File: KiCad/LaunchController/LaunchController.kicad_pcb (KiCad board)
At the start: 2 copper layers, 263 parts, among them J1 DC_IN, J10 CONN_SPEAKER, J11 CONN_EXT_I2C_0, J12 CONN_EXT_GPIO_0, J13 CONN_EXT_SPI_0, J14 CONN_EXT_I2C_1, J15 CONN_EXT_GPIO_1, J16 CONN_EXT_SPI_1, J17 CONN_USB, J18 CONN_EXT_I2C_2, J19 CONN_EXT_GPIO_2, J2 JMP_RUN, J20 USB_B_Micro, J21 CONN_EXT_SPI_2, J22 CONN_EXT_I2C_3, J23 CONN_EXT_GPIO_3, J24 JMP_DUMP, J25 JMP_SAFETY, J26 JMP_O2, J27 JMP_EMERGENCY_STOP, J28 JMP_IGNITOR, J29 JMP_SEQUENCE_START, J3 CONN_ICSP, J30 JMP_VALVE_OPEN, J31 JMP_FILL, J32 INDICATOR_PANEL, J33 JMP_VALVE_CLOSE, J34 JMP_PURGE, J35 CONTROL_PANEL, J36 STATUS_PANEL, J4 CONN_RS485, J5 JMP_KILL, J6 CONN_AUDIO, J7 L, J8 R, J9 CONN_EXT_UART, Q1 TJ8S06M3L, Q10 2SC3325-Y, Q11 2SC3325-Y, Q12 2SC3325-Y, Q13 2SC3325-Y, Q14 2SC3325-Y, Q2 TJ8S06M3L, Q3 2SC3325-Y, Q4 2SC3325-Y, Q5 2SC3325-Y, Q6 2SC3325-Y, Q7 2SC3325-Y, Q8 2SC3325-Y, Q9 2SC3325-Y, SW1 SW_RESET, U1 SI-8008HFE, U2 NJM7805SDL1, U3 INA219BIDCNT, U4 INA219BIDCNT, U5 U74HC14, U6 LTC485CN8#PBF, U7 FT232RL, U8 ATMEGA2560-16AUR, U9 U74HC14, Y1 HUSG-16.000-20

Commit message: ボード設計中（地獄）
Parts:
- R14: value 10kR -> 120R
- moved J4 255.6 mm to (261.6, 100.4), turned to -90 degrees
- moved J13 252.7 mm to (255.3, 141.0)
- moved J16 252.3 mm to (255.2, 148.0)
- moved J21 248.3 mm to (255.3, 154.9)
- moved R107 241.0 mm to (261.0, 35.3), turned to -90 degrees
- moved J11 240.0 mm to (241.3, 133.9)
- moved R106 237.6 mm to (258.4, 35.3), turned to -90 degrees
- moved J14 236.9 mm to (241.3, 141.0)
- moved J18 234.1 mm to (241.3, 148.0)
- moved J22 231.5 mm to (241.3, 154.9)
- moved J17 230.6 mm to (261.6, 69.7), turned to -90 degrees
- moved D21 229.3 mm to (263.5, 35.3), turned to -90 degrees
- moved J20 228.8 mm to (261.6, 59.4), turned to 90 degrees
- moved J9 228.1 mm to (213.4, 154.9)
- moved J12 224.2 mm to (227.4, 133.9)
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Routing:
- net LED_5V: track 0.00 -> 476.4 mm, vias 0 -> 17
- net SW_KILL: track 0.00 -> 195.4 mm, vias 0 -> 2
- net SW_PURGE: track 0.00 -> 123.2 mm
- net SW_VALVE_CLOSE: track 0.00 -> 114.5 mm
- net SW_VALVE_OPEN: track 0.00 -> 106.1 mm
- net SW_DUMP: track 0.00 -> 103.8 mm
- net I2C_SDA: track 0.00 -> 102.5 mm, vias 0 -> 3
- net I2C_SCL: track 0.00 -> 98.7 mm, vias 0 -> 4
- net SW_O2: track 0.00 -> 92.2 mm, vias 0 -> 1
- net SW_IGNITOR: track 0.00 -> 79.6 mm, vias 0 -> 1
- net SW_FILL: track 0.00 -> 76.6 mm
- net USB_VBUS: track 0.00 -> 72.4 mm, vias 0 -> 1
- net SW_SEQUENCE_START: track 0.00 -> 69.4 mm
- net LED_12V: track 0.00 -> 67.9 mm
- net SW_EMERGENCY_STOP: track 0.00 -> 63.4 mm
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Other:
- board outline added: 162.6 x 92.1 mm

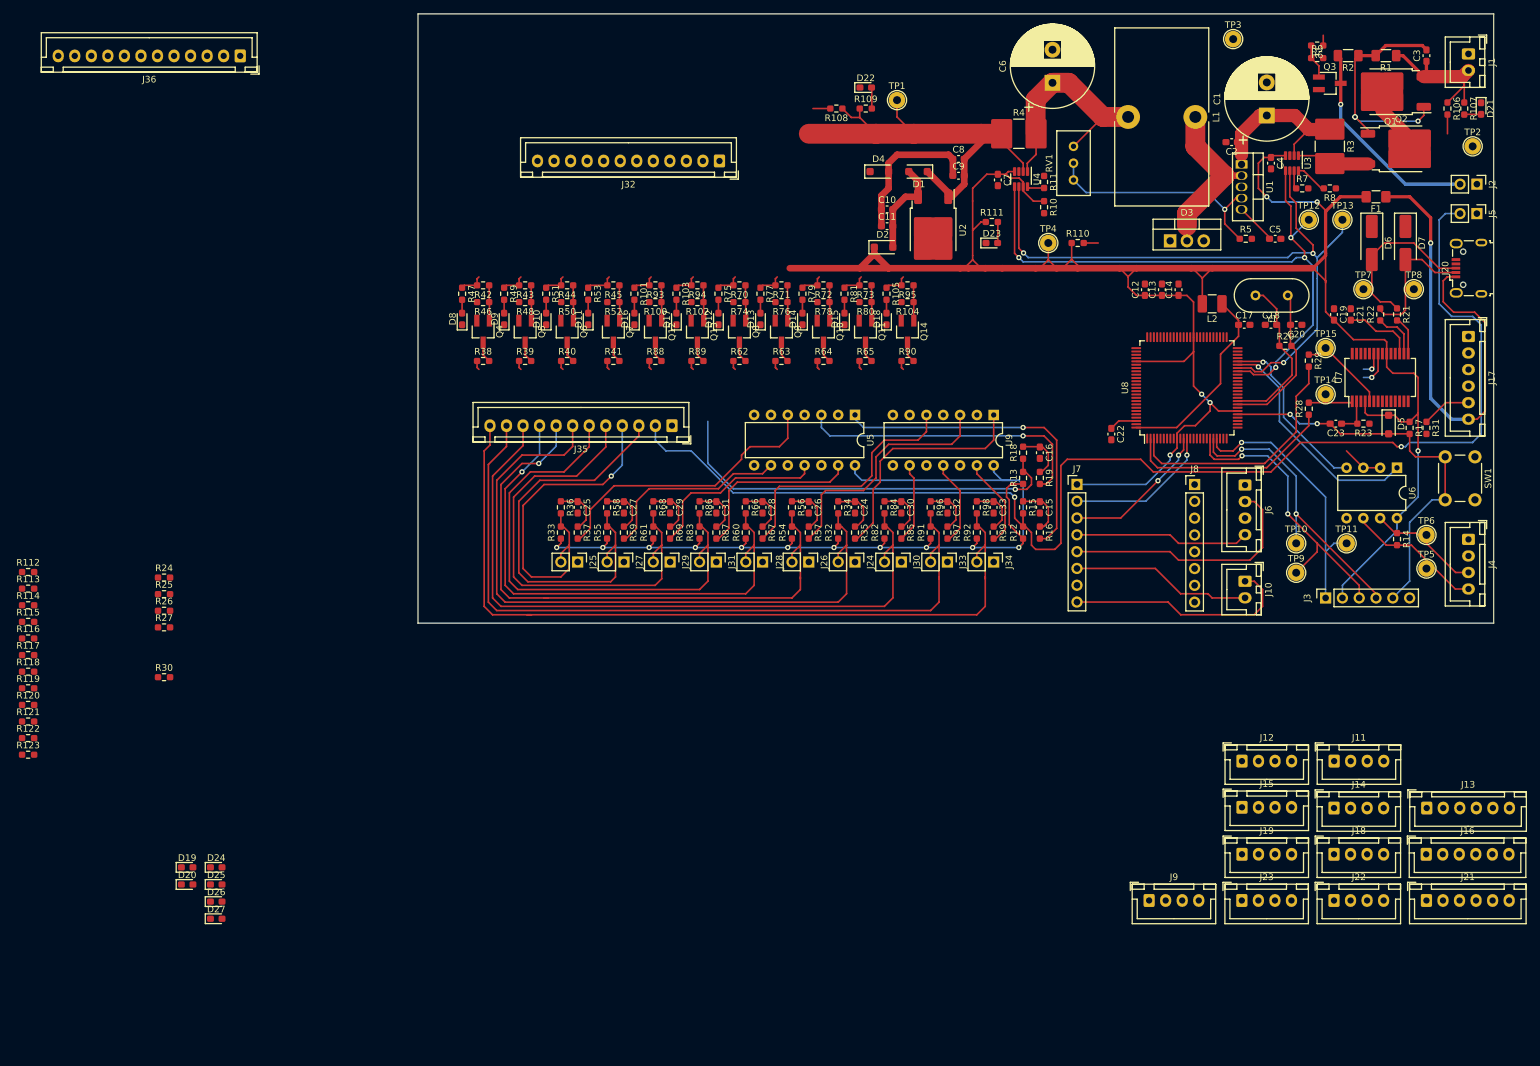
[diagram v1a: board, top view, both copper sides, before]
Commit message: 電圧から抵抗値を修正
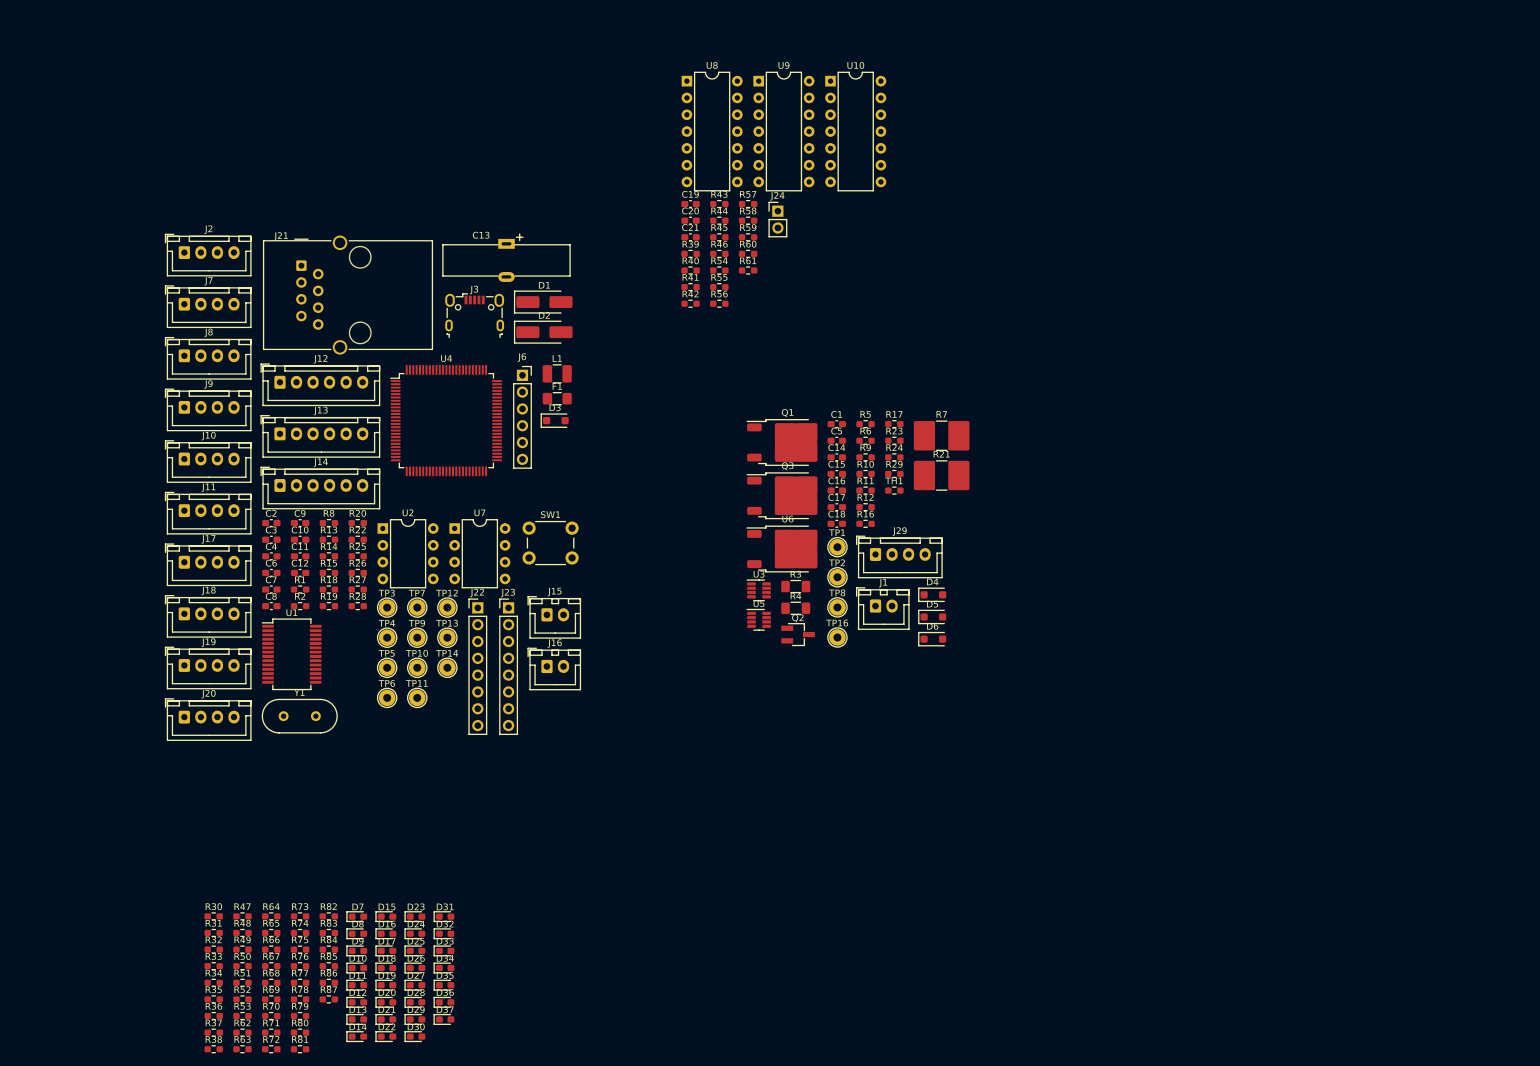
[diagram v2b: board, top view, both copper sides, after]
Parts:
- removed C22, C23, C24, C25, C26, C27, C28, C29, C30, C31, C32, C33: 0.1uF, Capacitor_SMD:C_0603_1608Metric_Pad1.08x0.95mm_HandSolder
- removed J25: JMP_SAFETY, Connector_PinHeader_2.54mm:PinHeader_1x02_P2.54mm_Vertical
- removed J26: JMP_O2, Connector_PinHeader_2.54mm:PinHeader_1x02_P2.54mm_Vertical
- removed J27: JMP_EMERGENCY_STOP, Connector_PinHeader_2.54mm:PinHeader_1x02_P2.54mm_Vertical
- removed J28: JMP_IGNITOR, Connector_PinHeader_2.54mm:PinHeader_1x02_P2.54mm_Vertical
- removed J30: JMP_VALVE_OPEN, Connector_PinHeader_2.54mm:PinHeader_1x02_P2.54mm_Vertical
- removed J31: JMP_FILL, Connector_PinHeader_2.54mm:PinHeader_1x02_P2.54mm_Vertical
- removed J32: INDICATOR_PANEL, Connector_JST:JST_XH_B12B-XH-A_1x12_P2.50mm_Vertical
- removed J33: JMP_VALVE_CLOSE, Connector_PinHeader_2.54mm:PinHeader_1x02_P2.54mm_Vertical
- removed J34: JMP_PURGE, Connector_PinHeader_2.54mm:PinHeader_1x02_P2.54mm_Vertical
- removed J35: CONTROL_PANEL, Connector_JST:JST_XH_B12B-XH-A_1x12_P2.50mm_Vertical
- removed J36: STATUS_PANEL, Connector_JST:JST_XH_B12B-XH-A_1x12_P2.50mm_Vertical
- removed J4: CONN_RS485, Connector_JST:JST_XH_B4B-XH-A_1x04_P2.50mm_Vertical
- removed J5: JMP_KILL, Connector_PinHeader_2.54mm:PinHeader_1x02_P2.54mm_Vertical
- removed L2: 10uH, Inductor_SMD:L_1210_3225Metric_Pad1.42x2.65mm_HandSolder
- removed Q10, Q11, Q12, Q13, Q14, Q4, Q5, Q6, Q7, Q8, Q9: 2SC3325-Y, Package_TO_SOT_SMD:SC-59_Handsoldering
- removed R100, R102, R104, R91, R92, R96, R98: 10kR, Resistor_SMD:R_0603_1608Metric_Pad0.98x0.95mm_HandSolder
- removed R101, R103, R105, R106, R107, R108, R109, R110, R111, R112, R113, R114, R115, R116, R117, R118, R119, R120, R121, R122, R123, R97, R99: 1kR, Resistor_SMD:R_0603_1608Metric_Pad0.98x0.95mm_HandSolder
- removed R88, R89, R90: 270R, Resistor_SMD:R_0603_1608Metric_Pad0.98x0.95mm_HandSolder
- removed R93, R94, R95: 2kR, Resistor_SMD:R_0603_1608Metric_Pad0.98x0.95mm_HandSolder
- removed RV1: 5kR, Potentiometer_THT:Potentiometer_Bourns_3296W_Vertical
- removed TP15: TP_TX0, TestPoint:TestPoint_THTPad_D2.5mm_Drill1.2mm
- added D28: LED, LED_SMD:LED_0603_1608Metric_Pad1.05x0.95mm_HandSolder, F.Cu at (102.6, 170.3)
- added D29: LED, LED_SMD:LED_0603_1608Metric_Pad1.05x0.95mm_HandSolder, F.Cu at (102.6, 172.9)
- added D30: LED, LED_SMD:LED_0603_1608Metric_Pad1.05x0.95mm_HandSolder, F.Cu at (102.6, 175.5)
- added D31: LED, LED_SMD:LED_0603_1608Metric_Pad1.05x0.95mm_HandSolder, F.Cu at (107.0, 157.4)
- added D32: LED, LED_SMD:LED_0603_1608Metric_Pad1.05x0.95mm_HandSolder, F.Cu at (107.0, 160.0)
- added D33: LED, LED_SMD:LED_0603_1608Metric_Pad1.05x0.95mm_HandSolder, F.Cu at (107.0, 162.6)
- added D34: LED, LED_SMD:LED_0603_1608Metric_Pad1.05x0.95mm_HandSolder, F.Cu at (107.0, 165.2)
- added D35: LED, LED_SMD:LED_0603_1608Metric_Pad1.05x0.95mm_HandSolder, F.Cu at (107.0, 167.7)
- added D36: LED, LED_SMD:LED_0603_1608Metric_Pad1.05x0.95mm_HandSolder, F.Cu at (107.0, 170.3)
- added D37: LED, LED_SMD:LED_0603_1608Metric_Pad1.05x0.95mm_HandSolder, F.Cu at (107.0, 172.9)
- added TH1: 10kR, Resistor_SMD:R_0603_1608Metric_Pad0.98x0.95mm_HandSolder, F.Cu at (174.9, 93.0)
- added TP16: TP_INPUT, TestPoint:TestPoint_THTPad_D2.5mm_Drill1.2mm, F.Cu at (166.3, 115.2)
- added U10: U74HC14, Package_DIP:DIP-14_W7.62mm, F.Cu at (165.2, 31.1)
- C1: value 1000uF -> 0.1uF; footprint Capacitor_THT:CP_Radial_D12.5mm_P5.00mm -> Capacitor_SMD:C_0603_1608Metric_Pad1.08x0.95mm_HandSolder
- C10, C8: value 10uF -> 0.1uF
- C13: value 0.1uF -> 1F; footprint Capacitor_SMD:C_0603_1608Metric_Pad1.08x0.95mm_HandSolder -> Capacitor_THT:DX_5R5VxxxxU_D19.0mm_P5.00mm
- C15, C17: value 0.1uF -> 10uF
- C18, C20: value 15pF -> 0.1uF
- C2: value 1uF -> 0.1uF
- C6: value 1000uF -> 15pF; footprint Capacitor_THT:CP_Radial_D12.5mm_P5.00mm -> Capacitor_SMD:C_0603_1608Metric_Pad1.08x0.95mm_HandSolder
- C7: value 0.1uF -> 15pF
- D1: value SS2040FL -> SMAJ45A; footprint Diode_SMD:D_SOD-123F -> Diode_SMD:D_SMA_Handsoldering
- D2: value GS1010FL -> SMAJ45A; footprint Diode_SMD:D_SOD-123F -> Diode_SMD:D_SMA_Handsoldering
- D3: value MBR3045FCT -> GS1010FL; footprint Package_TO_SOT_THT:TO-220-3_Vertical -> Diode_SMD:D_SOD-123F
- D5: value GS1010FL -> SS2040FL
- D6: value SMAJ45A -> SS2040FL; footprint Diode_SMD:D_SMA_Handsoldering -> Diode_SMD:D_SOD-123F
- D7: value SMAJ45A -> LED; footprint Diode_SMD:D_SMA_Handsoldering -> LED_SMD:LED_0603_1608Metric_Pad1.05x0.95mm_HandSolder
- J10: value CONN_SPEAKER -> CONN_EXT_I2C_2; footprint Connector_JST:JST_XH_B2B-XH-A_1x02_P2.50mm_Vertical -> Connector_JST:JST_XH_B4B-XH-A_1x04_P2.50mm_Vertical
- J11: value CONN_EXT_I2C_0 -> CONN_EXT_I2C_3
- J12: value CONN_EXT_GPIO_0 -> CONN_EXT_SPI_0; footprint Connector_JST:JST_XH_B4B-XH-A_1x04_P2.50mm_Vertical -> Connector_JST:JST_XH_B6B-XH-A_1x06_P2.50mm_Vertical
- J13: value CONN_EXT_SPI_0 -> CONN_EXT_SPI_1
- J14: value CONN_EXT_I2C_1 -> CONN_EXT_SPI_2; footprint Connector_JST:JST_XH_B4B-XH-A_1x04_P2.50mm_Vertical -> Connector_JST:JST_XH_B6B-XH-A_1x06_P2.50mm_Vertical
- J15: value CONN_EXT_GPIO_1 -> CONN_AUDIO; footprint Connector_JST:JST_XH_B4B-XH-A_1x04_P2.50mm_Vertical -> Connector_JST:JST_XH_B2B-XH-A_1x02_P2.50mm_Vertical
- J16: value CONN_EXT_SPI_1 -> CONN_SPEAKER; footprint Connector_JST:JST_XH_B6B-XH-A_1x06_P2.50mm_Vertical -> Connector_JST:JST_XH_B2B-XH-A_1x02_P2.50mm_Vertical
- J17: value CONN_USB -> CONN_EXT_GPIO_0; footprint Connector_JST:JST_XH_B6B-XH-A_1x06_P2.50mm_Vertical -> Connector_JST:JST_XH_B4B-XH-A_1x04_P2.50mm_Vertical
- J18: value CONN_EXT_I2C_2 -> CONN_EXT_GPIO_1
- J2: value JMP_RUN -> CONN_USB; footprint Connector_PinHeader_2.54mm:PinHeader_1x02_P2.54mm_Vertical -> Connector_JST:JST_XH_B4B-XH-A_1x04_P2.50mm_Vertical
- J20: value USB_B_Micro -> CONN_EXT_GPIO_3; footprint Connector_USB:USB_Micro-B_Wuerth_629105150521 -> Connector_JST:JST_XH_B4B-XH-A_1x04_P2.50mm_Vertical
- J21: value CONN_EXT_SPI_2 -> RJ45; footprint Connector_JST:JST_XH_B6B-XH-A_1x06_P2.50mm_Vertical -> Connector_RJ:RJ45_Wuerth_7499010001A_Horizontal
- J22: value CONN_EXT_I2C_3 -> L; footprint Connector_JST:JST_XH_B4B-XH-A_1x04_P2.50mm_Vertical -> Connector_PinHeader_2.54mm:PinHeader_1x08_P2.54mm_Vertical
- J23: value CONN_EXT_GPIO_3 -> R; footprint Connector_JST:JST_XH_B4B-XH-A_1x04_P2.50mm_Vertical -> Connector_PinHeader_2.54mm:PinHeader_1x08_P2.54mm_Vertical
- J24: value JMP_DUMP -> JMP_RUN
- J29: value JMP_SEQUENCE_START -> CONN_CONVERTER; footprint Connector_PinHeader_2.54mm:PinHeader_1x02_P2.54mm_Vertical -> Connector_JST:JST_XH_B4B-XH-A_1x04_P2.50mm_Vertical
- J3: value CONN_ICSP -> USB_B_Micro; footprint Connector_PinSocket_2.54mm:PinSocket_1x06_P2.54mm_Vertical -> Connector_USB:USB_Micro-B_Wuerth_629105150521
- J6: value CONN_AUDIO -> CONN_ICSP; footprint Connector_JST:JST_XH_B4B-XH-A_1x04_P2.50mm_Vertical -> Connector_PinSocket_2.54mm:PinSocket_1x06_P2.54mm_Vertical
- J7: value L -> CONN_EXT_UART; footprint Connector_PinHeader_2.54mm:PinHeader_1x08_P2.54mm_Vertical -> Connector_JST:JST_XH_B4B-XH-A_1x04_P2.50mm_Vertical
- J8: value R -> CONN_EXT_I2C_0; footprint Connector_PinHeader_2.54mm:PinHeader_1x08_P2.54mm_Vertical -> Connector_JST:JST_XH_B4B-XH-A_1x04_P2.50mm_Vertical
- J9: value CONN_EXT_UART -> CONN_EXT_I2C_1
- L1: value 100uH -> 10uH; footprint Inductor_THT:L_Toroid_Vertical_L26.7mm_W14.0mm_P10.16mm_Pulse_D -> Inductor_SMD:L_1210_3225Metric_Pad1.42x2.65mm_HandSolder
- Q2: value TJ8S06M3L -> 2SC3325-Y; footprint Package_TO_SOT_SMD:TO-252-2 -> Package_TO_SOT_SMD:SC-59_Handsoldering
- Q3: value 2SC3325-Y -> TJ8S06M3L; footprint Package_TO_SOT_SMD:SC-59_Handsoldering -> Package_TO_SOT_SMD:TO-252-2
- R1: value 560R1/2W -> 22R; footprint Resistor_SMD:R_1206_3216Metric_Pad1.30x1.75mm_HandSolder -> Resistor_SMD:R_0603_1608Metric_Pad0.98x0.95mm_HandSolder
- R11: value 10kR -> 12kR1/2W
- R12, R17: value 10kR -> 2kR1/2W
- R14: value 120R -> 1MR
- R15, R18, R34, R36, R46, R48, R50, R52, R54, R55, R56, R58, R60, R61, R66, R68, R74, R76, R78, R8, R80, R82, R83, R84, R86: value 10kR -> 1kR
- R16: value 1kR -> 12kR1/2W
- R2: value 330R1/2W -> 22R; footprint Resistor_SMD:R_1206_3216Metric_Pad1.30x1.75mm_HandSolder -> Resistor_SMD:R_0603_1608Metric_Pad0.98x0.95mm_HandSolder
- R20: value 1MR -> 10kR
- R21: value 22R -> 0.1R2W; footprint Resistor_SMD:R_0603_1608Metric_Pad0.98x0.95mm_HandSolder -> Resistor_SMD:R_2816_7142Metric_Pad3.20x4.45mm_HandSolder
- R22: value 22R -> 10kR
- R23, R29: value 1kR -> 10kR
- R25: value 10kR -> 4.7kR
- R28: value 1kR -> 120R
- R3: value 0.1R2W -> 560R1/2W; footprint Resistor_SMD:R_2816_7142Metric_Pad3.20x4.45mm_HandSolder -> Resistor_SMD:R_1206_3216Metric_Pad1.30x1.75mm_HandSolder
- R30: value 4.7kR -> 3.6kR
- R31: value 5.1kR -> 3.6kR
- R32, R33: value 10kR -> 2.4kR
- R38, R39, R40, R41, R62, R63, R64, R65: value 270R -> 1kR
- R4: value 0.1R2W -> 330R1/2W; footprint Resistor_SMD:R_2816_7142Metric_Pad3.20x4.45mm_HandSolder -> Resistor_SMD:R_1206_3216Metric_Pad1.30x1.75mm_HandSolder
- R42, R43, R44, R45, R70, R71, R72, R73: value 2kR -> 1kR
- R5: value 150R -> 10kR
- R7: value 10kR -> 0.1R2W; footprint Resistor_SMD:R_0603_1608Metric_Pad0.98x0.95mm_HandSolder -> Resistor_SMD:R_2816_7142Metric_Pad3.20x4.45mm_HandSolder
- TP10: value TP_MOSI -> TP_SDA
- TP11: value TP_MISO -> TP_RX0
- TP12: value TP_SCL -> TP_TX0
- TP13: value TP_SDA -> TP_A
- TP14: value TP_RX0 -> TP_B
- TP2: value TP_INPUT -> TP_GND
- TP3: value TP_GND -> TP_D+
- TP4: value TP_5V -> TP_D-
- TP5: value TP_A -> TP_SCK
- TP6: value TP_B -> TP_MOSI
- TP7: value TP_D+ -> TP_MISO
- TP8: value TP_D- -> TP_5V
- TP9: value TP_SCK -> TP_SCL
- U1: value SI-8008HFE -> FT232RL; footprint Package_TO_SOT_THT:TO-220-5_Vertical -> Package_SO:SSOP-28_5.3x10.2mm_P0.65mm
- U2: value NJM7805SDL1 -> 24LC256; footprint Package_TO_SOT_SMD:TO-252-2 -> Package_DIP:DIP-8_W7.62mm
- U4: value INA219BIDCNT -> ATMEGA2560-16AUR; footprint Package_TO_SOT_SMD:SOT-23-8 -> Package_QFP:TQFP-100_14x14mm_P0.5mm
- U5: value U74HC14 -> INA219BIDCNT; footprint Package_DIP:DIP-14_W7.62mm -> Package_TO_SOT_SMD:SOT-23-8
- U6: value LTC485CN8#PBF -> NJM7805SDL1; footprint Package_DIP:DIP-8_W7.62mm -> Package_TO_SOT_SMD:TO-252-2
- U7: value FT232RL -> LTC485CN8#PBF; footprint Package_SO:SSOP-28_5.3x10.2mm_P0.65mm -> Package_DIP:DIP-8_W7.62mm
- U8: value ATMEGA2560-16AUR -> U74HC14; footprint Package_QFP:TQFP-100_14x14mm_P0.5mm -> Package_DIP:DIP-14_W7.62mm
- moved D21 215.1 mm to (98.2, 172.9), turned to 0 degrees
- moved J20 205.6 mm to (67.6, 127.2), turned to 0 degrees
- moved R31 198.5 mm to (72.0, 159.8), turned to 0 degrees
- moved J17 197.0 mm to (67.6, 103.8), turned to 0 degrees
- moved J2 195.6 mm to (67.6, 57.0), turned to 0 degrees
- moved J21 195.2 mm to (85.2, 59.0)
- moved C3 189.3 mm to (80.7, 100.4), turned to 0 degrees
- moved D7 188.2 mm to (93.8, 157.4), turned to 0 degrees
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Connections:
- net CTL_IGNITOR renamed CTL_SHIFT
- net Net-(C28-Pad1) renamed LED_LOW_VOLTAGE
- C1 pad 1: Net-(U1-VIN) -> LED_INPUT
- C1 pad 2: USB_GND -> Net-(Q1-G)
- C10 pad 1: Net-(D4-A) -> Net-(U4-AVCC)
- C10 pad 2: Net-(D1-A) -> USB_GND
- C11 pad 1: Net-(D4-A) -> LED_5V
- C11 pad 2: Net-(D1-A) -> USB_GND
- C15 pad 1: Net-(C15-Pad1) -> Net-(D5-A)
- C15 pad 2: USB_GND -> LED_12V
- C16 pad 1: Net-(C16-Pad1) -> Net-(D5-A)
- C16 pad 2: USB_GND -> LED_12V
- C17 pad 1: Net-(U8-AVCC) -> Net-(D5-A)
- C17 pad 2: USB_GND -> Net-(D4-A)
- C18 pad 1: USB_GND -> Net-(D5-A)
- C18 pad 2: Net-(U8-XTAL1) -> Net-(D4-A)
- C2 pad 1: Net-(U1-VIN) -> USB_GND
- C2 pad 2: USB_GND -> Net-(U1-3V3OUT)
- C20 pad 2: Net-(U8-XTAL2) -> LED_5V
- C21 pad 2: Net-(U7-3V3OUT) -> LED_5V
- C3 pad 1: LED_INPUT -> USB_GND
- C3 pad 2: Net-(Q1-G) -> LED_5V
- C4 pad 1: LED_5V -> Net-(U1-DTR)
- C4 pad 2: USB_GND -> CTL_RESET
- C5 pad 1: Net-(U1-~{ON}/OFF) -> LED_5V
- C6 pad 1: Net-(U4-IN+) -> USB_GND
- C6 pad 2: USB_GND -> Net-(U4-XTAL1)
- C7 pad 1: LED_5V -> USB_GND
- C7 pad 2: USB_GND -> Net-(U4-XTAL2)
- C8 pad 1: Net-(D4-A) -> Net-(U4-AREF)
- C8 pad 2: LED_12V -> USB_GND
- C9 pad 1: Net-(D4-A) -> LED_5V
- C9 pad 2: LED_12V -> USB_GND
- D1 pad 1: LED_12V -> USB_GND
- D1 pad 2: Net-(D1-A) -> USB_D+
- D14 pad 1: USB_GND -> Net-(D14-K)
- D14 pad 2: Net-(D14-A) -> LED_5V
- D15 pad 1: USB_GND -> Net-(D15-K)
- D15 pad 2: Net-(D15-A) -> LED_5V
- D19 pad 1: Net-(D19-K) -> USB_GND
- D19 pad 2: LED_5V -> Net-(D19-A)
- D2 pad 1: LED_5V -> USB_GND
- D2 pad 2: Net-(D1-A) -> USB_D-
- D20 pad 1: Net-(D20-K) -> USB_GND
- D20 pad 2: LED_5V -> Net-(D20-A)
- D3 pad 1: USB_GND -> LED_5V
- D3 pad 2: Net-(D3-A) -> CTL_RESET
- D4 pad 1: USB_GND -> LED_12V
- D5 pad 1: LED_5V -> USB_GND
- D5 pad 2: CTL_RESET -> Net-(D5-A)
- D6 pad 1: USB_GND -> LED_5V
- D6 pad 2: USB_D+ -> Net-(D4-A)
- D7 pad 2: USB_D- -> Net-(D7-A)
- J10 pad 1: Net-(J10-Pin_1) -> USB_GND
- J10 pad 2: Net-(J10-Pin_2) -> I2C_SCL
- J12 pad 2: EXT_GPIO_01 -> SPI_CS_EXT0
- J12 pad 3: EXT_GPIO_00 -> SPI_MOSI
- J12 pad 4: LED_5V -> SPI_SCK
- J13 pad 2: SPI_CS_EXT0 -> SPI_CS_EXT1
- J14 pad 2: I2C_SCL -> SPI_CS_EXT2
- J14 pad 3: I2C_SDA -> SPI_MOSI
- J14 pad 4: LED_5V -> SPI_SCK
- J15 pad 2: EXT_GPIO_11 -> Net-(J15-Pin_2)
- J16 pad 1: USB_GND -> Net-(J16-Pin_1)
- J16 pad 2: SPI_CS_EXT1 -> Net-(J16-Pin_2)
- J17 pad 2: USB_GND -> EXT_GPIO_01
- J17 pad 3: USB_D+ -> EXT_GPIO_00
- J17 pad 4: USB_D- -> LED_5V
- J18 pad 2: I2C_SCL -> EXT_GPIO_11
- J18 pad 3: I2C_SDA -> EXT_GPIO_10
- J2 pad 2: CTL_RUN -> USB_D+
- J20 pad 1: USB_VBUS -> USB_GND
- J20 pad 2: USB_D- -> EXT_GPIO_31
- J20 pad 3: USB_D+ -> EXT_GPIO_30
- J20 pad 4: unconnected-(J20-ID-Pad4) -> LED_5V
- J21 pad 2: SPI_CS_EXT2 -> USB_GND
- J21 pad 3: SPI_MOSI -> USB_GND
- J21 pad 4: SPI_SCK -> Net-(U7-A)
- J21 pad 5: SPI_MISO -> Net-(U7-B)
- J21 pad 6: LED_5V -> USB_GND
- J22 pad 1: USB_GND -> LED_5V
- J22 pad 2: I2C_SCL -> UART2_TX
- J22 pad 3: I2C_SDA -> UART2_RX
- J22 pad 4: LED_5V -> unconnected-(J22-Pin_4-Pad4)
- J23 pad 1: USB_GND -> unconnected-(J23-Pin_1-Pad1)
- J23 pad 2: EXT_GPIO_31 -> unconnected-(J23-Pin_2-Pad2)
- J23 pad 3: EXT_GPIO_30 -> unconnected-(J23-Pin_3-Pad3)
- J23 pad 4: LED_5V -> unconnected-(J23-Pin_4-Pad4)
- J24 pad 2: SW_DUMP -> CTL_RUN
- J29 pad 1: USB_GND -> FROM_CONVERTER
- J29 pad 2: SW_SEQUENCE_START -> USB_GND
- J3 pad 1: SPI_MISO -> USB_VBUS
- J3 pad 2: LED_5V -> USB_D-
- J3 pad 3: SPI_SCK -> USB_D+
- J3 pad 4: SPI_MOSI -> unconnected-(J3-ID-Pad4)
- J3 pad 5: CTL_RESET -> USB_GND
- J3 pad 6: USB_GND -> USB_SHIELD
- J6 pad 1: USB_GND -> SPI_MISO
- J6 pad 2: Net-(J6-Pin_2) -> LED_5V
- J6 pad 3: USB_GND -> SPI_SCK
- J6 pad 4: Net-(J6-Pin_4) -> SPI_MOSI
- J7 pad 1: LED_5V -> USB_GND
- J7 pad 2: UART2_TX -> UART3_RX
- J7 pad 3: UART2_RX -> UART3_TX
- J7 pad 4: Net-(J6-Pin_4) -> LED_5V
- J8 pad 1: unconnected-(J8-Pin_1-Pad1) -> USB_GND
- J8 pad 2: unconnected-(J8-Pin_2-Pad2) -> I2C_SCL
- J8 pad 3: unconnected-(J8-Pin_3-Pad3) -> I2C_SDA
- J8 pad 4: unconnected-(J8-Pin_4-Pad4) -> LED_5V
- J9 pad 2: UART3_RX -> I2C_SCL
- J9 pad 3: UART3_TX -> I2C_SDA
- L1 pad 1: Net-(D3-A) -> Net-(U4-AVCC)
- L1 pad 2: Net-(U4-IN+) -> LED_5V
- Q2 pad 1: Net-(Q1-G) -> Net-(Q2-B)
- Q2 pad 2: Net-(Q1-D) -> USB_GND
- Q2 pad 3: +VSW -> CTL_RUN
- Q3 pad 1: Net-(Q3-B) -> Net-(Q1-G)
- Q3 pad 2: USB_GND -> Net-(Q1-D)
- Q3 pad 3: CTL_RUN -> +VSW
- R1 pad 1: LED_INPUT -> USB_D+
- R1 pad 2: Net-(Q1-G) -> Net-(U1-USBD+)
- R10 pad 1: LED_5V -> USB_GND
- R10 pad 2: USB_GND -> Net-(U3-A1)
- R11 pad 1: USB_GND -> VREF_VSW
- R11 pad 2: Net-(U4-A1) -> +VSW
- R12 pad 1: LED_5V -> USB_GND
- R12 pad 2: SW_KILL -> VREF_VSW
- R13 pad 2: SW_RESET -> CTL_RESET
- R14 pad 1: Net-(J4-Pin_3) -> Net-(U4-XTAL1)
- R14 pad 2: Net-(J4-Pin_4) -> Net-(U4-XTAL2)
- R15 pad 1: Net-(C15-Pad1) -> UART2_RX
- R15 pad 2: SW_KILL -> Net-(U4-PH0)
- R16 pad 1: Net-(C15-Pad1) -> VREF_12V
- R16 pad 2: Net-(R16-Pad2) -> LED_12V
- R17 pad 1: LED_5V -> USB_GND
- R17 pad 2: CTL_RESET -> VREF_12V
- R18 pad 1: SW_RESET -> Net-(U4-PE0)
- R18 pad 2: Net-(C16-Pad1) -> UART0_RX
- R19 pad 1: Net-(C16-Pad1) -> UART0_TX
- R19 pad 2: Net-(R19-Pad2) -> Net-(U4-PE1)
- R2 pad 1: Net-(Q1-G) -> Net-(U1-USBD-)
- R2 pad 2: CTL_RUN -> USB_D-
- R20 pad 1: Net-(U8-XTAL1) -> LED_5V
- R20 pad 2: Net-(U8-XTAL2) -> I2C_SCL
- R21 pad 1: USB_D+ -> LED_12V
- R21 pad 2: Net-(U7-USBD+) -> FROM_CONVERTER
- R22 pad 1: Net-(U7-USBD-) -> LED_5V
- R22 pad 2: USB_D- -> I2C_SDA
- R23 pad 1: Net-(U7-DTR) -> LED_5V
- R24 pad 1: LED_5V -> USB_GND
- R24 pad 2: I2C_SCL -> Net-(U5-A1)
- R25 pad 1: LED_5V -> SPI_CS_EXT0
- R25 pad 2: I2C_SDA -> LED_5V
- R26 pad 1: SPI_CS_EXT0 -> SPI_CS_EXT1
- R27 pad 1: SPI_CS_EXT1 -> SPI_CS_EXT2
- R28 pad 1: Net-(U8-PE0) -> Net-(U7-B)
- R28 pad 2: UART0_RX -> Net-(U7-A)
- R29 pad 1: UART0_TX -> USB_GND
- R29 pad 2: Net-(U8-PE1) -> VREF_THERMISTOR
- R3 pad 1: Net-(U1-VIN) -> LED_INPUT
- R3 pad 2: +VSW -> Net-(Q1-G)
- R30 pad 1: SPI_CS_EXT2 -> LED_INPUT
- R30 pad 2: LED_5V -> CONN_LED_INPUT
- R31 pad 1: USB_CC -> LED_INPUT
- R31 pad 2: USB_GND -> Net-(D7-A)
- R32 pad 1: LED_5V -> LED_12V
- R32 pad 2: SW_DUMP -> CONN_LED_12V
- R33 pad 1: LED_5V -> LED_12V
- R33 pad 2: SW_SAFETY -> Net-(D8-A)
- R34 pad 1: Net-(C24-Pad1) -> LED_5V
- R34 pad 2: SW_DUMP -> CONN_LED_5V
- R35 pad 1: Net-(C24-Pad1) -> LED_5V
- R35 pad 2: Net-(R35-Pad2) -> Net-(D9-A)
- R36 pad 1: Net-(C25-Pad1) -> LED_RS485_TX
- R36 pad 2: SW_SAFETY -> CONN_LED_RS485_TX
- R37 pad 1: Net-(C25-Pad1) -> LED_RS485_TX
- R37 pad 2: Net-(R37-Pad2) -> Net-(D10-A)
- R38 pad 1: CONN_LED_POWER -> LED_RS485_RX
- R38 pad 2: Net-(Q4-C) -> CONN_LED_RS485_RX
- R39 pad 1: CONN_LED_SAFTEY -> SW_KILL
- R39 pad 2: Net-(Q5-C) -> Net-(R39-Pad2)
- R4 pad 1: LED_12V -> Net-(Q1-G)
- R4 pad 2: Net-(U4-IN+) -> CTL_RUN
- R40 pad 1: CONN_LED_SEQUENCE -> SW_SAFETY
- R40 pad 2: Net-(Q6-C) -> Net-(R40-Pad2)
- R41 pad 1: CONN_LED_CONFIRM -> SW_SEQUENCE_START
- R41 pad 2: Net-(Q7-C) -> Net-(R41-Pad2)
- R42 pad 1: Net-(Q4-B) -> SW_EMERGENCY_STOP
- R42 pad 2: LED_POWER -> Net-(R42-Pad2)
- R43 pad 1: Net-(Q5-B) -> SW_CONFIRM_1
- R43 pad 2: LED_SAFTEY -> Net-(R43-Pad2)
- R44 pad 1: Net-(Q6-B) -> SW_CONFIRM_2
- R44 pad 2: LED_SEQUENCE -> Net-(R44-Pad2)
- R45 pad 1: Net-(Q7-B) -> SW_CONFIRM_3
- R45 pad 2: LED_CONFIRM -> Net-(R45-Pad2)
- R46 pad 1: Net-(Q4-B) -> SW_RESET
- R46 pad 2: USB_GND -> Net-(R46-Pad2)
- R47 pad 1: LED_POWER -> LED_RS485_RX
- R47 pad 2: Net-(D8-A) -> Net-(D11-A)
- R48 pad 1: Net-(Q5-B) -> LED_COM
- R48 pad 2: USB_GND -> CONN_LED_COM
- R49 pad 1: LED_SAFTEY -> LED_COM
- R49 pad 2: Net-(D9-A) -> Net-(D12-A)
- R5 pad 1: Net-(U1-FB) -> Net-(Q2-B)
- R50 pad 1: Net-(Q6-B) -> LED_TASK
- R50 pad 2: USB_GND -> CONN_LED_TASK
- R51 pad 1: LED_SEQUENCE -> LED_TASK
- R51 pad 2: Net-(D10-A) -> Net-(D13-A)
- R52 pad 1: Net-(Q7-B) -> CONN_LED_USB_TX
- R52 pad 2: USB_GND -> LED_USB_TX
- R53 pad 1: LED_CONFIRM -> Net-(D14-K)
- R53 pad 2: Net-(D11-A) -> LED_USB_TX
- R54 pad 1: LED_5V -> SW_SHIFT
- R54 pad 2: SW_O2 -> Net-(R54-Pad2)
- R55 pad 1: LED_5V -> SW_FILL
- R55 pad 2: SW_EMERGENCY_STOP -> Net-(R55-Pad2)
- R56 pad 1: Net-(C26-Pad1) -> SW_DUMP
- R56 pad 2: SW_O2 -> Net-(R56-Pad2)
- R57 pad 1: Net-(C26-Pad1) -> SW_O2
- R58 pad 1: Net-(C27-Pad1) -> SW_IGNITOR
- R58 pad 2: SW_EMERGENCY_STOP -> Net-(R58-Pad2)
- R59 pad 1: Net-(C27-Pad1) -> SW_OPEN
- R6 pad 2: Net-(Q3-B) -> Net-(Q2-B)
- R60 pad 1: LED_5V -> SW_CLOSE
- R60 pad 2: SW_IGNITOR -> Net-(R60-Pad2)
- R61 pad 1: LED_5V -> SW_PURGE
- R61 pad 2: SW_SEQUENCE_START -> Net-(R61-Pad2)
- R62 pad 1: CONN_LED_O2 -> CONN_LED_USB_RX
- R62 pad 2: Net-(Q8-C) -> LED_USB_RX
- R63 pad 1: CONN_LED_IGNITOR -> Net-(D15-K)
- R63 pad 2: Net-(Q9-C) -> LED_USB_RX
- R64 pad 1: CONN_LED_VALVE_OPEN -> LED_CAUTION
- R64 pad 2: Net-(Q10-C) -> CONN_LED_CAUTION
- R65 pad 1: CONN_LED_VALVE_CLOSE -> LED_CAUTION
- R65 pad 2: Net-(Q11-C) -> Net-(D16-A)
- R66 pad 2: SW_IGNITOR -> CONN_LED_LOW_VOLTAGE
- R67 pad 2: Net-(R67-Pad2) -> Net-(D17-A)
- R68 pad 1: Net-(C29-Pad1) -> CONN_LED_POWER
- R68 pad 2: SW_SEQUENCE_START -> Net-(D18-A)
- R69 pad 1: Net-(C29-Pad1) -> CONN_LED_SHIFT
- R69 pad 2: Net-(R69-Pad2) -> Net-(D19-A)
- R7 pad 1: Net-(U3-A0) -> TO_CONVERTER
- R7 pad 2: USB_GND -> +VSW
- R70 pad 1: Net-(Q8-B) -> CONN_LED_FB_SHIFT
- R70 pad 2: LED_O2 -> Net-(D20-A)
- R71 pad 1: Net-(Q9-B) -> CONN_LED_SAFTEY
- R71 pad 2: LED_IGNITOR -> Net-(D21-A)
- R72 pad 1: Net-(Q10-B) -> CONN_LED_FILL
- R72 pad 2: LED_VALVE_OPEN -> Net-(D22-A)
- R73 pad 1: Net-(Q11-B) -> CONN_LED_FB_FILL
- R73 pad 2: LED_VALVE_CLOSE -> Net-(D23-A)
- R74 pad 1: Net-(Q8-B) -> CONN_LED_SEQUENCE
- R74 pad 2: USB_GND -> Net-(D24-A)
- R75 pad 1: LED_O2 -> CONN_LED_DUMP
- R75 pad 2: Net-(D12-A) -> Net-(D25-A)
- R76 pad 1: Net-(Q9-B) -> CONN_LED_FB_DUMP
- R76 pad 2: USB_GND -> Net-(D26-A)
- R77 pad 1: LED_IGNITOR -> CONN_LED_EMERGENCY
- R77 pad 2: Net-(D13-A) -> Net-(D27-A)
- R78 pad 1: Net-(Q10-B) -> CONN_LED_O2
- R78 pad 2: USB_GND -> Net-(D28-A)
- R79 pad 1: LED_VALVE_OPEN -> CONN_FB_LED_O2
- R79 pad 2: Net-(D14-A) -> Net-(D29-A)
- R8 pad 1: USB_GND -> Net-(U1-DTR)
- R8 pad 2: Net-(U3-A1) -> USB_GND
- R80 pad 1: Net-(Q11-B) -> CONN_LED_IGNITOR
- R80 pad 2: USB_GND -> Net-(D30-A)
- R81 pad 1: LED_VALVE_CLOSE -> CONN_LED_FB_IGNITOR
- R81 pad 2: Net-(D15-A) -> Net-(D31-A)
- R82 pad 1: LED_5V -> CONN_LED_OPEN
- R82 pad 2: SW_VALVE_OPEN -> Net-(D32-A)
- R83 pad 1: LED_5V -> CONN_LED_FB_OPEN
- R83 pad 2: SW_FILL -> Net-(D33-A)
- R84 pad 1: Net-(C30-Pad1) -> CONN_LED_CLOSE
- R84 pad 2: SW_VALVE_OPEN -> Net-(D34-A)
- R85 pad 1: Net-(C30-Pad1) -> CONN_LED_FB_CLOSE
- R85 pad 2: Net-(R85-Pad2) -> Net-(D35-A)
- R86 pad 1: Net-(C31-Pad1) -> CONN_LED_PURGE
- R86 pad 2: SW_FILL -> Net-(D36-A)
- R87 pad 1: Net-(C31-Pad1) -> CONN_LED_FB_PURGE
- R87 pad 2: Net-(R87-Pad2) -> Net-(D37-A)
- R9 pad 1: Net-(Q3-B) -> Net-(U3-A0)
- TP10 pad 1: SPI_MOSI -> I2C_SDA
- TP11 pad 1: SPI_MISO -> UART0_RX
- TP12 pad 1: I2C_SCL -> UART0_TX
- TP13 pad 1: I2C_SDA -> Net-(U7-A)
- TP14 pad 1: UART0_RX -> Net-(U7-B)
- TP2 pad 1: LED_INPUT -> USB_GND
- TP3 pad 1: USB_GND -> USB_D+
- TP4 pad 1: LED_5V -> USB_D-
- TP5 pad 1: Net-(J4-Pin_4) -> SPI_SCK
- TP6 pad 1: Net-(J4-Pin_3) -> SPI_MOSI
- TP7 pad 1: USB_D+ -> SPI_MISO
- TP8 pad 1: USB_D- -> LED_5V
- TP9 pad 1: SPI_SCK -> I2C_SCL
- U1 pad 1: Net-(U1-VIN) -> UART0_RX
- U1 pad 2: Net-(D3-A) -> Net-(U1-DTR)
- U1 pad 3: USB_GND -> unconnected-(U1-RTS-Pad3)
- U1 pad 4: Net-(U1-FB) -> LED_5V
- U1 pad 5: Net-(U1-~{ON}/OFF) -> UART0_TX
- U2 pad 1: LED_12V -> USB_GND
- U2 pad 2: Net-(D4-A) -> USB_GND
- U2 pad 3: Net-(D1-A) -> USB_GND
- U3 pad 2: Net-(U1-VIN) -> TO_CONVERTER
- U4 pad 1: Net-(U4-IN+) -> unconnected-(U4-PG5-Pad1)
- U4 pad 2: LED_12V -> Net-(U4-PE0)
- U4 pad 3: USB_GND -> Net-(U4-PE1)
- U4 pad 4: LED_5V -> unconnected-(U4-PE2-Pad4)
- U4 pad 5: I2C_SCL -> unconnected-(U4-PE3-Pad5)
- U4 pad 6: I2C_SDA -> unconnected-(U4-PE4-Pad6)
- U4 pad 7: LED_5V -> unconnected-(U4-PE5-Pad7)
- U4 pad 8: Net-(U4-A1) -> unconnected-(U4-PE6-Pad8)
- U5 pad 1: Net-(R16-Pad2) -> FROM_CONVERTER
- U5 pad 2: CTL_KILL -> LED_12V
- U5 pad 3: Net-(R19-Pad2) -> USB_GND
- U5 pad 4: CTL_RESET -> LED_5V
- U5 pad 5: Net-(R37-Pad2) -> I2C_SCL
- U5 pad 6: CTL_SAFETY -> I2C_SDA
- U5 pad 7: USB_GND -> LED_5V
- U5 pad 8: CTL_EMERGENCY_STOP -> Net-(U5-A1)
- U6 pad 1: UART1_RX -> LED_12V
- U6 pad 2: CTL_RS485_DERE -> Net-(D5-A)
- U6 pad 3: CTL_RS485_DERE -> Net-(D4-A)
- U7 pad 1: UART0_RX -> UART1_RX
- U7 pad 2: Net-(U7-DTR) -> CTL_RS485_DERE
- U7 pad 3: unconnected-(U7-RTS-Pad3) -> CTL_RS485_DERE
- U7 pad 4: LED_5V -> UART1_TX
- U7 pad 5: UART0_TX -> USB_GND
- U7 pad 6: unconnected-(U7-RI-Pad6) -> Net-(U7-A)
- U7 pad 7: USB_GND -> Net-(U7-B)
- U7 pad 8: (no net) -> LED_5V
- U8 pad 1: unconnected-(U8-PG5-Pad1) -> Net-(R39-Pad2)
- U8 pad 10: LED_5V -> CTL_CONFIRM_1
- U8 pad 11: USB_GND -> Net-(R43-Pad2)
- U8 pad 12: UART2_RX -> CTL_CONFIRM_2
- U8 pad 13: UART2_TX -> Net-(R44-Pad2)
- U8 pad 14: unconnected-(U8-PH2-Pad14) -> LED_5V
- U8 pad 2: Net-(U8-PE0) -> CTL_KILL
- U8 pad 3: Net-(U8-PE1) -> Net-(R40-Pad2)
- U8 pad 4: unconnected-(U8-PE2-Pad4) -> CTL_SAFETY
- U8 pad 5: unconnected-(U8-PE3-Pad5) -> Net-(R41-Pad2)
- U8 pad 6: unconnected-(U8-PE4-Pad6) -> CTL_SEQUENCE_START
- U8 pad 7: unconnected-(U8-PE5-Pad7) -> USB_GND
- U8 pad 8: unconnected-(U8-PE6-Pad8) -> CTL_EMERGENCY_STOP
- U8 pad 9: unconnected-(U8-PE7-Pad9) -> Net-(R42-Pad2)
- U9 pad 1: Net-(R35-Pad2) -> Net-(R45-Pad2)
- U9 pad 10: CTL_VALVE_CLOSE -> CTL_DUMP
- U9 pad 11: Net-(R97-Pad2) -> Net-(R56-Pad2)
- U9 pad 12: CTL_PURGE -> CTL_O2
- U9 pad 13: Net-(R99-Pad2) -> Net-(R57-Pad2)
- U9 pad 2: CTL_DUMP -> CTL_CONFIRM_3
- U9 pad 3: Net-(R57-Pad2) -> Net-(R46-Pad2)
- U9 pad 4: CTL_O2 -> CTL_RESET
- U9 pad 5: Net-(R67-Pad2) -> Net-(R54-Pad2)
- U9 pad 8: CTL_VALVE_OPEN -> CTL_FILL
- U9 pad 9: Net-(R85-Pad2) -> Net-(R55-Pad2)
- Y1 pad 1: Net-(U8-XTAL2) -> Net-(U4-XTAL2)
- Y1 pad 2: Net-(U8-XTAL1) -> Net-(U4-XTAL1)
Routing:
- net LED_5V: track 476.4 -> 0.00 mm, vias 17 -> 0
- net SW_KILL: track 195.4 -> 0.00 mm, vias 2 -> 0
- net SW_PURGE: track 123.2 -> 0.00 mm
- net SW_VALVE_CLOSE: track 114.5 -> 0.00 mm
- net SW_VALVE_OPEN: track 106.1 -> 0.00 mm
- net SW_DUMP: track 103.8 -> 0.00 mm
- net I2C_SDA: track 102.5 -> 0.00 mm, vias 3 -> 0
- net I2C_SCL: track 98.7 -> 0.00 mm, vias 4 -> 0
- net SW_O2: track 92.2 -> 0.00 mm, vias 1 -> 0
- net SW_IGNITOR: track 79.6 -> 0.00 mm, vias 1 -> 0
- net SW_FILL: track 76.6 -> 0.00 mm
- net USB_VBUS: track 72.4 -> 0.00 mm, vias 1 -> 0
- net SW_SEQUENCE_START: track 69.4 -> 0.00 mm
- net LED_12V: track 67.9 -> 0.00 mm
- net SW_EMERGENCY_STOP: track 63.4 -> 0.00 mm
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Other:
- board outline removed

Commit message: 基板寸法を設定
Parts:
- removed D18, D19, D20, D21, D22, D23, D24, D25, D26, D27, D28, D29, D30, D31, D32, D33, D34, D35, D36, D37: LED, LED_SMD:LED_0603_1608Metric_Pad1.05x0.95mm_HandSolder
- removed J22: L, Connector_PinHeader_2.54mm:PinHeader_1x08_P2.54mm_Vertical
- removed J23: R, Connector_PinHeader_2.54mm:PinHeader_1x08_P2.54mm_Vertical
- removed J24: JMP_RUN, Connector_PinHeader_2.54mm:PinHeader_1x02_P2.54mm_Vertical
- removed R68, R69, R70, R71, R72, R73, R74, R75, R76, R77, R78, R79, R80, R81, R82, R83, R84, R85, R86, R87: 1kR, Resistor_SMD:R_0603_1608Metric_Pad0.98x0.95mm_HandSolder
- added J4: CONN_AUDIO, Connector_JST:JST_XH_B2B-XH-A_1x02_P2.50mm_Vertical, F.Cu at (-43.9, 108.4)
- added J5: CONN_SPEAKER, Connector_JST:JST_XH_B2B-XH-A_1x02_P2.50mm_Vertical, F.Cu at (-43.9, 116.2)
- added R88: 1kR, Resistor_SMD:R_0603_1608Metric_Pad0.98x0.95mm_HandSolder, F.Cu at (-89.7, 194.8)
- added REF**: MountingHole_3.2mm_M3, MountingHole:MountingHole_3.2mm_M3, F.Cu at (84.2, 124.0)
- added REF**: MountingHole_3.2mm_M3, MountingHole:MountingHole_3.2mm_M3, F.Cu at (184.2, 78.0)
- added REF**: MountingHole_3.2mm_M3, MountingHole:MountingHole_3.2mm_M3, F.Cu at (84.2, 78.0)
- added REF**: MountingHole_3.2mm_M3, MountingHole:MountingHole_3.2mm_M3, F.Cu at (184.2, 124.0)
- J10: value CONN_EXT_I2C_2 -> CONN_EXT_UART
- J11: value CONN_EXT_I2C_3 -> CONN_EXT_I2C_0
- J12: value CONN_EXT_SPI_0 -> CONN_EXT_I2C_1; footprint Connector_JST:JST_XH_B6B-XH-A_1x06_P2.50mm_Vertical -> Connector_JST:JST_XH_B4B-XH-A_1x04_P2.50mm_Vertical
- J13: value CONN_EXT_SPI_1 -> CONN_EXT_I2C_2; footprint Connector_JST:JST_XH_B6B-XH-A_1x06_P2.50mm_Vertical -> Connector_JST:JST_XH_B4B-XH-A_1x04_P2.50mm_Vertical
- J14: value CONN_EXT_SPI_2 -> CONN_EXT_I2C_3; footprint Connector_JST:JST_XH_B6B-XH-A_1x06_P2.50mm_Vertical -> Connector_JST:JST_XH_B4B-XH-A_1x04_P2.50mm_Vertical
- J15: value CONN_AUDIO -> CONN_EXT_SPI_0; footprint Connector_JST:JST_XH_B2B-XH-A_1x02_P2.50mm_Vertical -> Connector_JST:JST_XH_B6B-XH-A_1x06_P2.50mm_Vertical
- J16: value CONN_SPEAKER -> CONN_EXT_SPI_1; footprint Connector_JST:JST_XH_B2B-XH-A_1x02_P2.50mm_Vertical -> Connector_JST:JST_XH_B6B-XH-A_1x06_P2.50mm_Vertical
- J17: value CONN_EXT_GPIO_0 -> CONN_EXT_SPI_2; footprint Connector_JST:JST_XH_B4B-XH-A_1x04_P2.50mm_Vertical -> Connector_JST:JST_XH_B6B-XH-A_1x06_P2.50mm_Vertical
- J18: value CONN_EXT_GPIO_1 -> CONN_EXT_GPIO_0
- J19: value CONN_EXT_GPIO_2 -> CONN_EXT_GPIO_1
- J20: value CONN_EXT_GPIO_3 -> CONN_EXT_GPIO_2
- J21: value RJ45 -> CONN_EXT_GPIO_3; footprint Connector_RJ:RJ45_Wuerth_7499010001A_Horizontal -> Connector_JST:JST_XH_B4B-XH-A_1x04_P2.50mm_Vertical
- J7: value CONN_EXT_UART -> L; footprint Connector_JST:JST_XH_B4B-XH-A_1x04_P2.50mm_Vertical -> Connector_PinHeader_2.54mm:PinHeader_1x08_P2.54mm_Vertical
- J8: value CONN_EXT_I2C_0 -> R; footprint Connector_JST:JST_XH_B4B-XH-A_1x04_P2.50mm_Vertical -> Connector_PinHeader_2.54mm:PinHeader_1x08_P2.54mm_Vertical
- J9: value CONN_EXT_I2C_1 -> RJ45; footprint Connector_JST:JST_XH_B4B-XH-A_1x04_P2.50mm_Vertical -> Connector_RJ:RJ45_Wuerth_7499010001A_Horizontal
- R25: value 4.7kR -> 120R
- R28: value 120R -> 4.7kR
- moved R57 286.3 mm to (-94.1, 194.8)
- moved R43 283.8 mm to (-98.4, 189.8)
- moved R44 283.8 mm to (-98.4, 192.3)
- moved R45 283.8 mm to (-98.4, 194.8)
- moved U9 281.4 mm to (-92.5, 166.2)
- moved C19 281.4 mm to (-102.8, 184.8)
- moved C20 281.4 mm to (-102.8, 187.3)
- moved C21 281.4 mm to (-102.8, 189.8)
- moved R39 281.4 mm to (-102.8, 192.3)
- moved R40 281.4 mm to (-102.8, 194.8)
- moved U10 281.4 mm to (-81.6, 166.2)
- moved U8 281.4 mm to (-103.3, 166.2)
- moved R58 276.4 mm to (-89.7, 184.8)
- moved R59 276.4 mm to (-89.7, 187.3)
- moved R60 276.4 mm to (-89.7, 189.8)
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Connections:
- J10 pad 2: I2C_SCL -> UART3_RX
- J10 pad 3: I2C_SDA -> UART3_TX
- J12 pad 2: SPI_CS_EXT0 -> I2C_SCL
- J12 pad 3: SPI_MOSI -> I2C_SDA
- J12 pad 4: SPI_SCK -> LED_5V
- J13 pad 2: SPI_CS_EXT1 -> I2C_SCL
- J13 pad 3: SPI_MOSI -> I2C_SDA
- J13 pad 4: SPI_SCK -> LED_5V
- J14 pad 2: SPI_CS_EXT2 -> I2C_SCL
- J14 pad 3: SPI_MOSI -> I2C_SDA
- J14 pad 4: SPI_SCK -> LED_5V
- J15 pad 2: Net-(J15-Pin_2) -> SPI_CS_EXT0
- J16 pad 1: Net-(J16-Pin_1) -> USB_GND
- J16 pad 2: Net-(J16-Pin_2) -> SPI_CS_EXT1
- J17 pad 2: EXT_GPIO_01 -> SPI_CS_EXT2
- J17 pad 3: EXT_GPIO_00 -> SPI_MOSI
- J17 pad 4: LED_5V -> SPI_SCK
- J18 pad 2: EXT_GPIO_11 -> EXT_GPIO_01
- J18 pad 3: EXT_GPIO_10 -> EXT_GPIO_00
- J19 pad 2: EXT_GPIO_21 -> EXT_GPIO_11
- J19 pad 3: EXT_GPIO_20 -> EXT_GPIO_10
- J20 pad 2: EXT_GPIO_31 -> EXT_GPIO_21
- J20 pad 3: EXT_GPIO_30 -> EXT_GPIO_20
- J21 pad 2: USB_GND -> EXT_GPIO_31
- J21 pad 3: USB_GND -> EXT_GPIO_30
- J21 pad 4: Net-(U7-A) -> LED_5V
- J7 pad 1: USB_GND -> LED_5V
- J7 pad 2: UART3_RX -> UART2_TX
- J7 pad 3: UART3_TX -> UART2_RX
- J7 pad 4: LED_5V -> unconnected-(J7-Pin_4-Pad4)
- J8 pad 1: USB_GND -> unconnected-(J8-Pin_1-Pad1)
- J8 pad 2: I2C_SCL -> unconnected-(J8-Pin_2-Pad2)
- J8 pad 3: I2C_SDA -> unconnected-(J8-Pin_3-Pad3)
- J8 pad 4: LED_5V -> unconnected-(J8-Pin_4-Pad4)
- J9 pad 2: I2C_SCL -> USB_GND
- J9 pad 3: I2C_SDA -> USB_GND
- J9 pad 4: LED_5V -> Net-(U7-A)
- R25 pad 1: SPI_CS_EXT0 -> Net-(U7-B)
- R25 pad 2: LED_5V -> Net-(U7-A)
- R26 pad 1: SPI_CS_EXT1 -> SPI_CS_EXT0
- R27 pad 1: SPI_CS_EXT2 -> SPI_CS_EXT1
- R28 pad 1: Net-(U7-B) -> SPI_CS_EXT2
- R28 pad 2: Net-(U7-A) -> LED_5V
- U10 pad 1: Net-(R58-Pad2) -> Net-(R57-Pad2)
- U10 pad 10: (no net) -> CTL_PURGE
- U10 pad 11: (no net) -> Net-(R61-Pad2)
- U10 pad 2: CTL_IGNITOR -> CTL_O2
- U10 pad 3: Net-(R59-Pad2) -> Net-(R58-Pad2)
- U10 pad 4: CTL_OPEN -> CTL_IGNITOR
- U10 pad 5: Net-(R60-Pad2) -> Net-(R59-Pad2)
- U10 pad 6: CTL_CLOSE -> CTL_OPEN
- U10 pad 8: CTL_PURGE -> CTL_CLOSE
- U10 pad 9: Net-(R61-Pad2) -> Net-(R60-Pad2)
- U8 pad 1: Net-(R39-Pad2) -> Net-(R88-Pad2)
- U8 pad 10: CTL_CONFIRM_1 -> CTL_EMERGENCY_STOP
- U8 pad 11: Net-(R43-Pad2) -> Net-(R42-Pad2)
- U8 pad 12: CTL_CONFIRM_2 -> CTL_CONFIRM_1
- U8 pad 13: Net-(R44-Pad2) -> Net-(R43-Pad2)
- U8 pad 2: CTL_KILL -> CTL_RUN
- U8 pad 3: Net-(R40-Pad2) -> Net-(R39-Pad2)
- U8 pad 4: CTL_SAFETY -> CTL_KILL
- U8 pad 5: Net-(R41-Pad2) -> Net-(R40-Pad2)
- U8 pad 6: CTL_SEQUENCE_START -> CTL_SAFETY
- U8 pad 8: CTL_EMERGENCY_STOP -> CTL_SEQUENCE_START
- U8 pad 9: Net-(R42-Pad2) -> Net-(R41-Pad2)
- U9 pad 1: Net-(R45-Pad2) -> Net-(R44-Pad2)
- U9 pad 10: CTL_DUMP -> CTL_FILL
- U9 pad 11: Net-(R56-Pad2) -> Net-(R55-Pad2)
- U9 pad 12: CTL_O2 -> CTL_DUMP
- U9 pad 13: Net-(R57-Pad2) -> Net-(R56-Pad2)
- U9 pad 2: CTL_CONFIRM_3 -> CTL_CONFIRM_2
- U9 pad 3: Net-(R46-Pad2) -> Net-(R45-Pad2)
- U9 pad 4: CTL_RESET -> CTL_CONFIRM_3
- U9 pad 5: Net-(R54-Pad2) -> Net-(R46-Pad2)
- U9 pad 6: CTL_SHIFT -> CTL_RESET
- U9 pad 8: CTL_FILL -> CTL_SHIFT
- U9 pad 9: Net-(R55-Pad2) -> Net-(R54-Pad2)
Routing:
- added copper zone on B.Cu, net USB_GND
- added copper zone on F.Cu, net USB_GND
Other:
- board outline added: 120 x 66 mm
- board text added: "内寸"
- board text added: "変圧"
